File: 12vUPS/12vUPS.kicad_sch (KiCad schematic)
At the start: 15 parts, among them J1 INPUT, J2 BATTERY, J3 OUTPUT, J4 ENABLE, K1 VEGHA L08A0212VDC, Q1 BDX53C

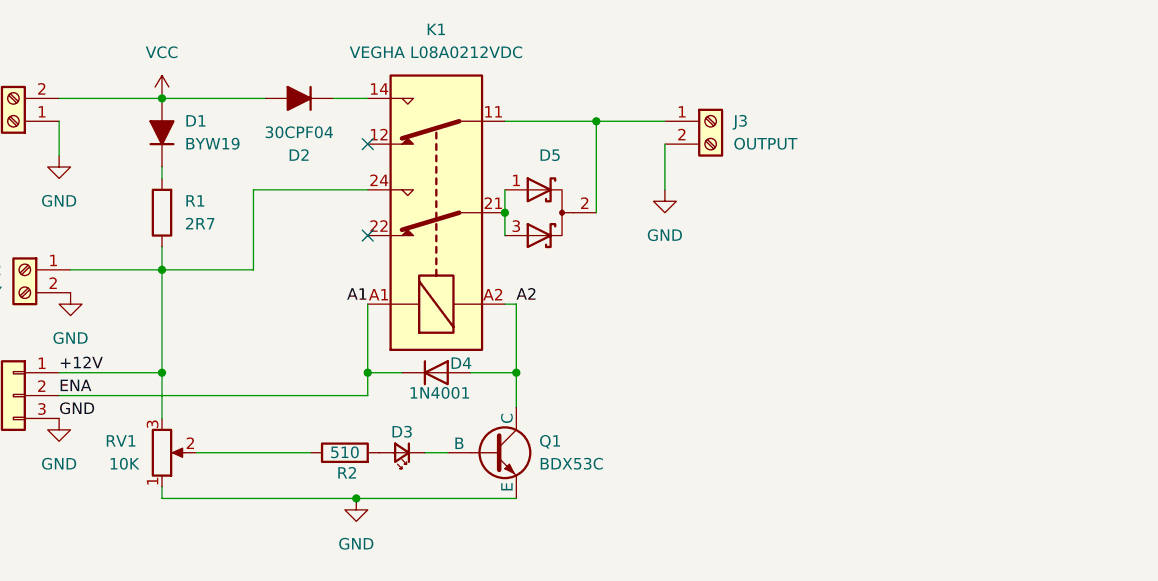
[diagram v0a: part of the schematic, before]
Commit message: Update 12vUPS-2025-06-08_110639.zip, 12vUPS-2025-06-08_231957.zip, 12vUPS-2025-06-08_232518.zip, and 11 more files
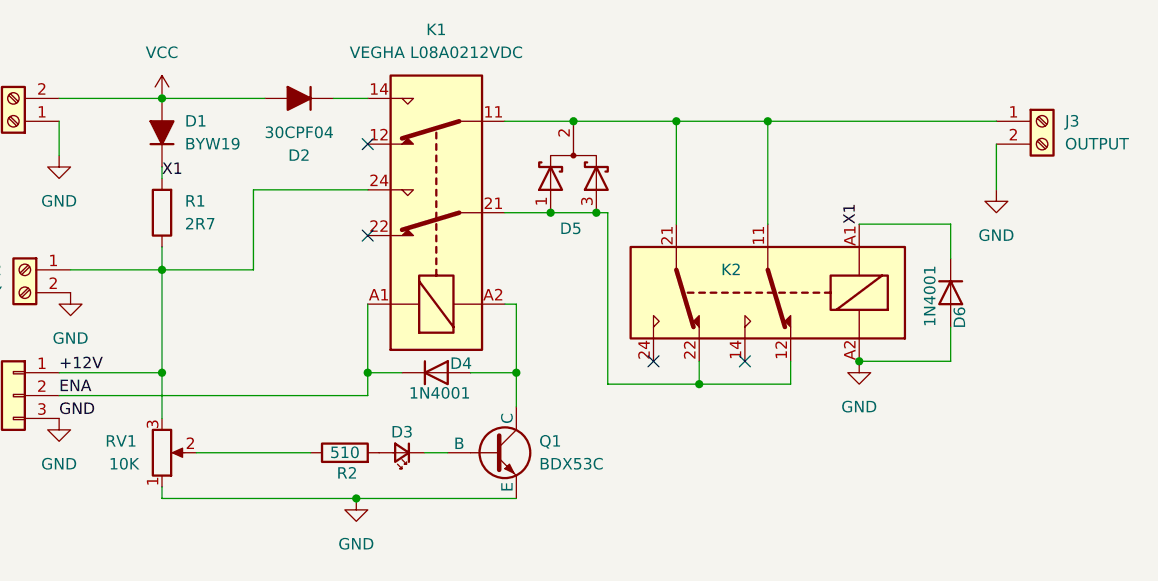
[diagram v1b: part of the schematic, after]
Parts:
- added D6: 1N4001, Diode_THT:D_A-405_P10.16mm_Horizontal, symbol Device:D
- added K2: VEGHA L08A0212VDC, IK5PWC:VEGhA L08 12V dc, symbol Relay:Relay_DPDT
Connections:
- net GND: now also D6.2 (A), K2.A2
- net at D3.1 (K): now also Q1.1 (B); no longer Q1.2 (B)
- net at D5.2 (K), J3.1 (Pin_1), K1.11: now also K2.11, K2.21
- net at D5.1 (A), D5.3 (A), K1.21: now also K2.12, K2.22
- net X1: now reaches D1.1 (K), R1.2
- net X1: now also D6.1 (K), K2.A1
- net A1 renamed ENA
- net A2: no longer names the net of D4.2 (A), K1.A2
- net A2: now also Q1.2 (C); no longer Q1.1 (C)
- no-connect marks 3 -> 5
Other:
- moved on the sheet: D5, J3

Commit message: Update 12vUPS-2025-06-10_185612.zip, 12vUPS-2025-06-10_190121.zip, 12vUPS-2025-06-10_190645.zip, and 3 more files
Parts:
- removed D5: D_Schottky_Dual_CommonCathode_AKA_Parallel, Package_TO_SOT_THT:TO-247-3_Vertical, symbol Device:D_Schottky_Dual_CommonCathode_AKA_Parallel
- removed D6: 1N4001, Diode_THT:D_A-405_P10.16mm_Horizontal, symbol Device:D
- removed K2: VEGHA L08A0212VDC, IK5PWC:VEGhA L08 12V dc, symbol Relay:Relay_DPDT
- added D6: W01G, Diode_THT:Diode_Bridge_Round_D9.8mm, symbol Diode_Bridge:W01G
- added D7: D_Ideal, symbol IK5PWC:D_Ideal
- Q1: symbol Simulation_SPICE:NPN -> Transistor_BJT:Q_NPN_BCE
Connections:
- net GND: now also D7.3 (GND)
- net OUT: now reaches J3.1 (Pin_1), K1.11
- net OUT: now also D6.2, D7.1 (K)
- net at K1.21: now also D7.2 (A)
- net at D3.2 (A): now also R2.1; no longer R2.2
- net at RV1.2: now also R2.2; no longer R2.1
- net +12V renamed BATT
- net BATT: no longer RV1.3
- net VCC renamed INPUT
- net INPUT: now also D6.4
- net X1: no longer names the net of D1.1 (K), R1.2
- new net: D6.1 (+), RV1.3
- no-connect marks 5 -> 4
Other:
- moved on the sheet: D1, D2, D3, J1, J2, J3, J4, R1, R2, RV1
